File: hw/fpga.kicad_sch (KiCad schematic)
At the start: 39 parts, among them U7712 ECP5-LFE5U-12, Y7702 40MHz

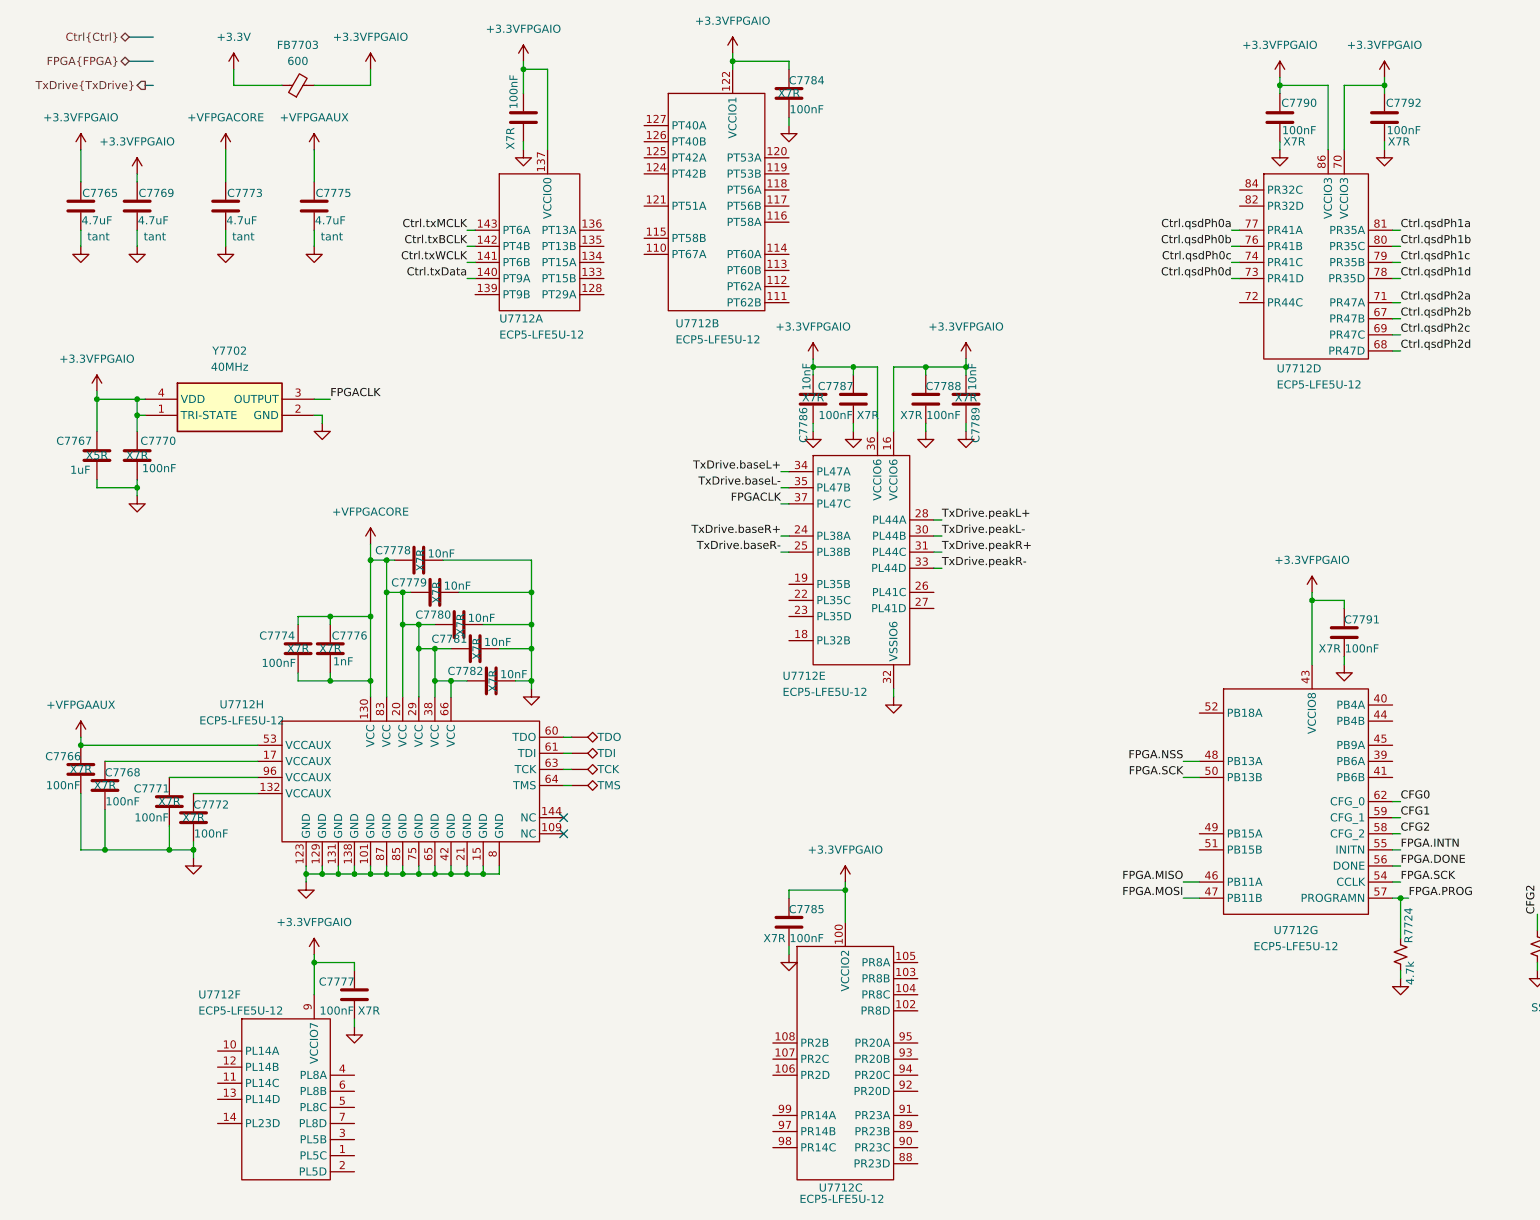
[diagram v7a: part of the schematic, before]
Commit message: All symbols and footprints seem right now, and schematic again imports into PCB without error
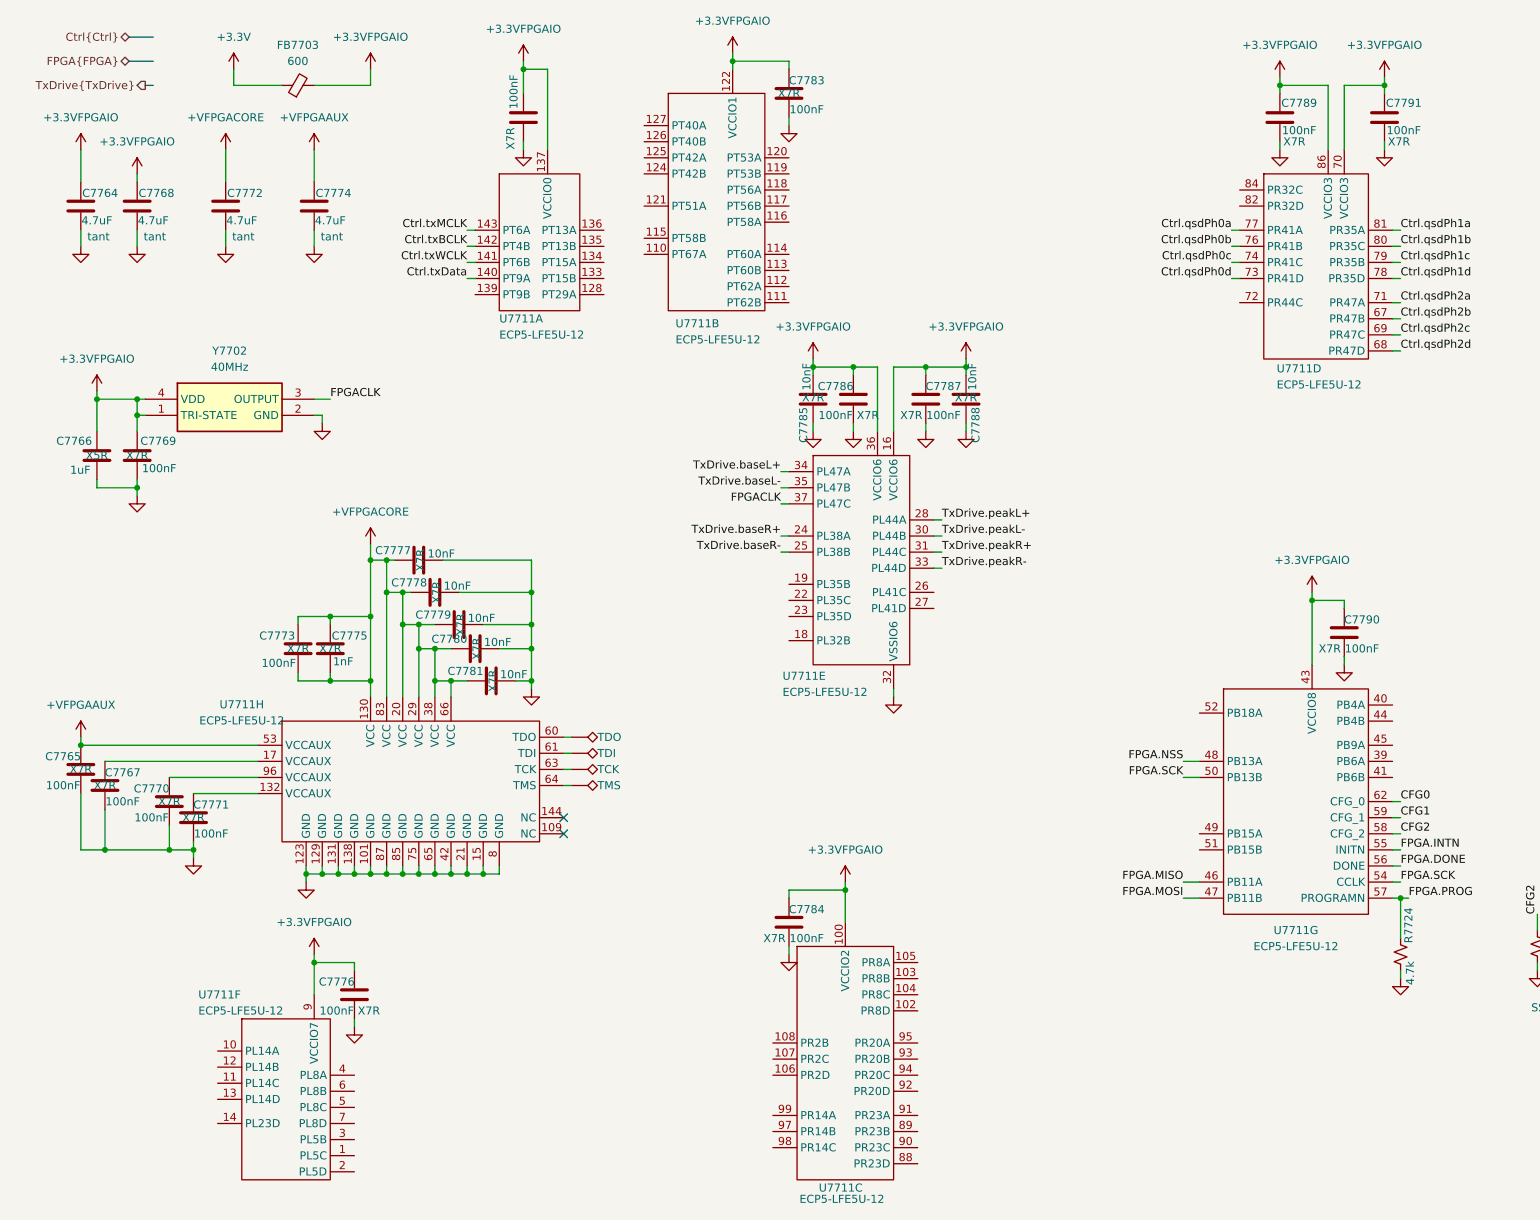
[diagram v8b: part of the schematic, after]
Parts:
- renumbered C7765 to C7764, C7766 to C7765, C7767 to C7766, C7768 to C7767, C7769 to C7768, C7770 to C7769, C7771 to C7770, C7772 to C7771, C7773 to C7772, C7774 to C7773, C7775 to C7774, C7776 to C7775, C7777 to C7776, C7778 to C7777, C7779 to C7778, C7780 to C7779, C7781 to C7780, C7782 to C7781, C7783 to C7782, C7784 to C7783, C7785 to C7784, C7786 to C7785, C7787 to C7786, C7788 to C7787, C7789 to C7788, C7790 to C7789, C7791 to C7790, C7792 to C7791, U7712 to U7711
